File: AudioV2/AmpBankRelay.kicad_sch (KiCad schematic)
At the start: 20 parts, among them K301 AZ850P2-5, K302 AZ850P2-5, K303 AZ850P2-5, K304 AZ850P2-5, U321 TBD62083APG

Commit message: AudioV2: AmpBankSwitch に MCP/ADDR を寄せ、親の SLOT SEL を外す
娘で SEL を出し、縦積み向け ADDR ジャンパと PCB デジタル島・AMP_SEL 取り回しを進める。

Co-authored-by: Cursor <cursoragent@cursor.com>
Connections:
- net CH1_RST: now also U_IO302.27 (GPA6); no longer U_IO302.1 (GPB0)
- net CH1_SET: now also U_IO302.28 (GPA7); no longer U_IO302.21 (GPA0)
- net CH2_RST: now also U_IO302.25 (GPA4); no longer U_IO302.2 (GPB1)
- net CH2_SET: now also U_IO302.26 (GPA5); no longer U_IO302.22 (GPA1)
- net CH3_RST: now also U_IO302.23 (GPA2); no longer U_IO302.3 (GPB2)
- net CH3_SET: now also U_IO302.24 (GPA3); no longer U_IO302.23 (GPA2)
- net CH4_RST: now also U_IO302.21 (GPA0); no longer U_IO302.4 (GPB3)
- net CH4_SET: now also U_IO302.22 (GPA1); no longer U_IO302.24 (GPA3)

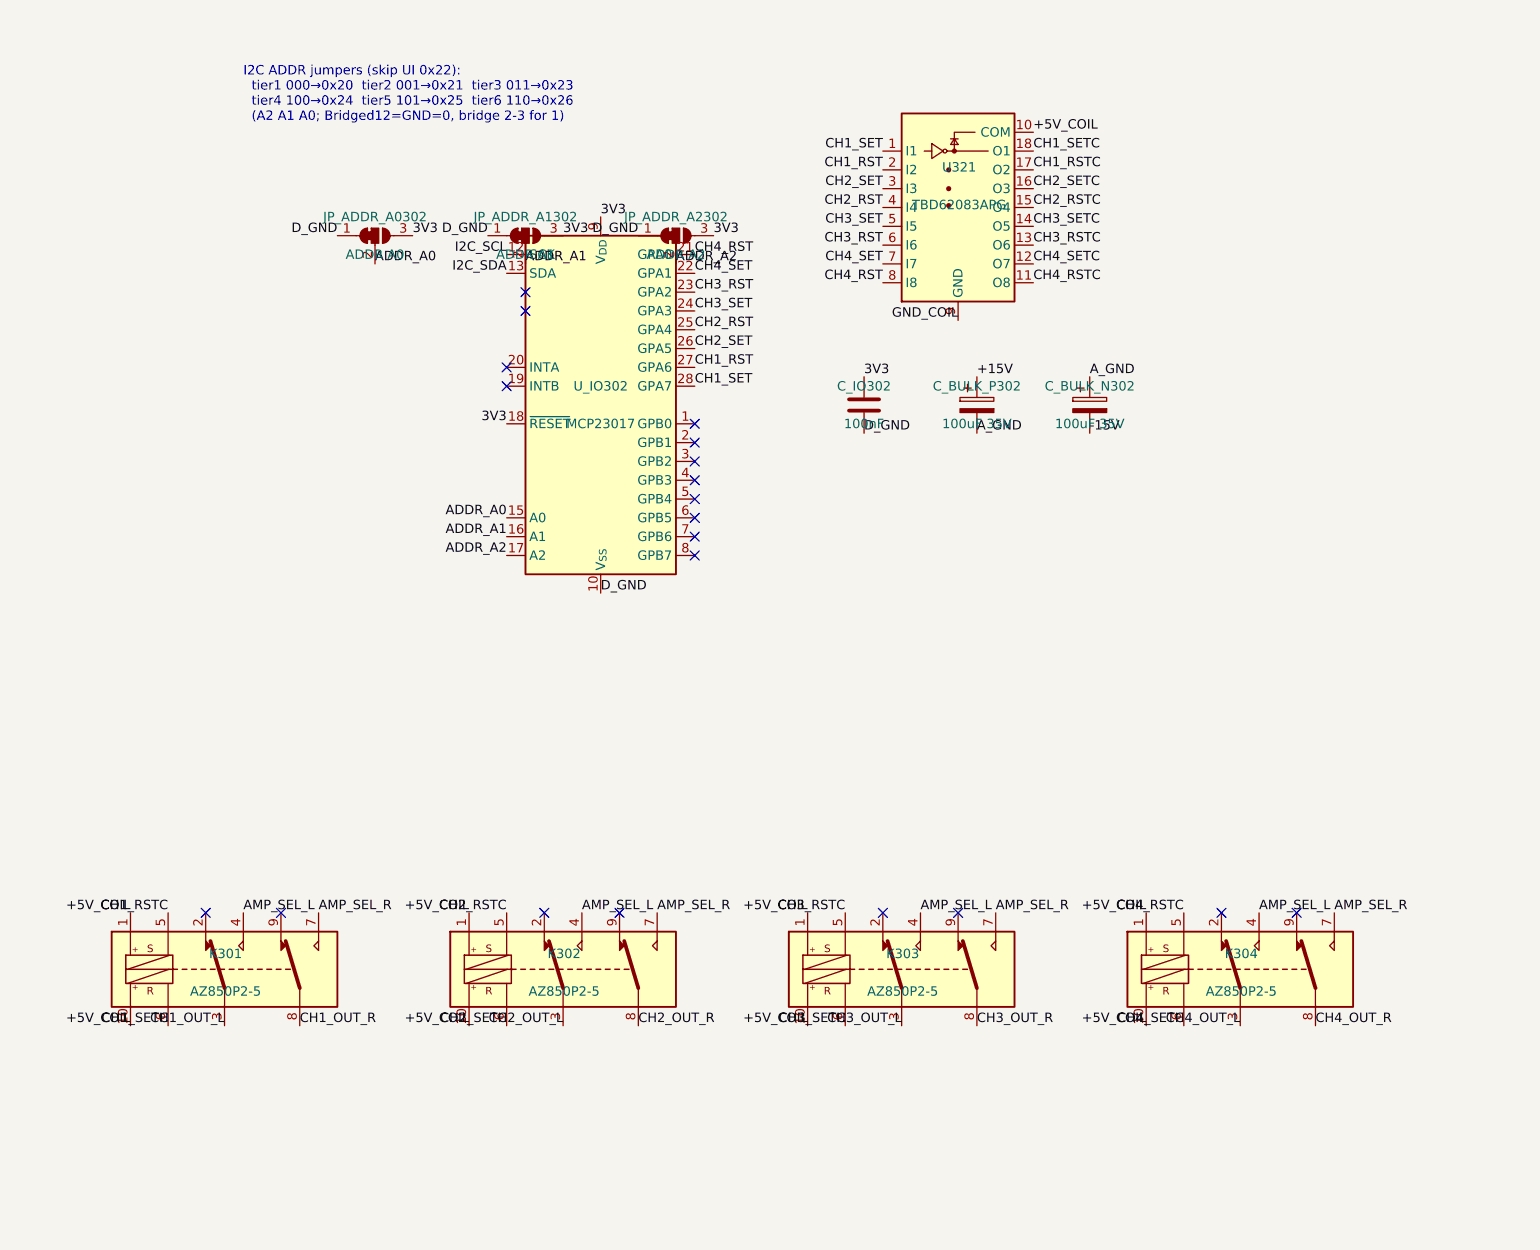
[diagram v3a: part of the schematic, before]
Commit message: AudioV2: AmpBankRelay の配置・配線と回路図更新を保存
CH を横並び＋K 南向きに整え、局所配線まで閉じた。外形拡幅と
回路図側のラベル／接続の直しも同梱する。

Co-authored-by: Cursor <cursoragent@cursor.com>
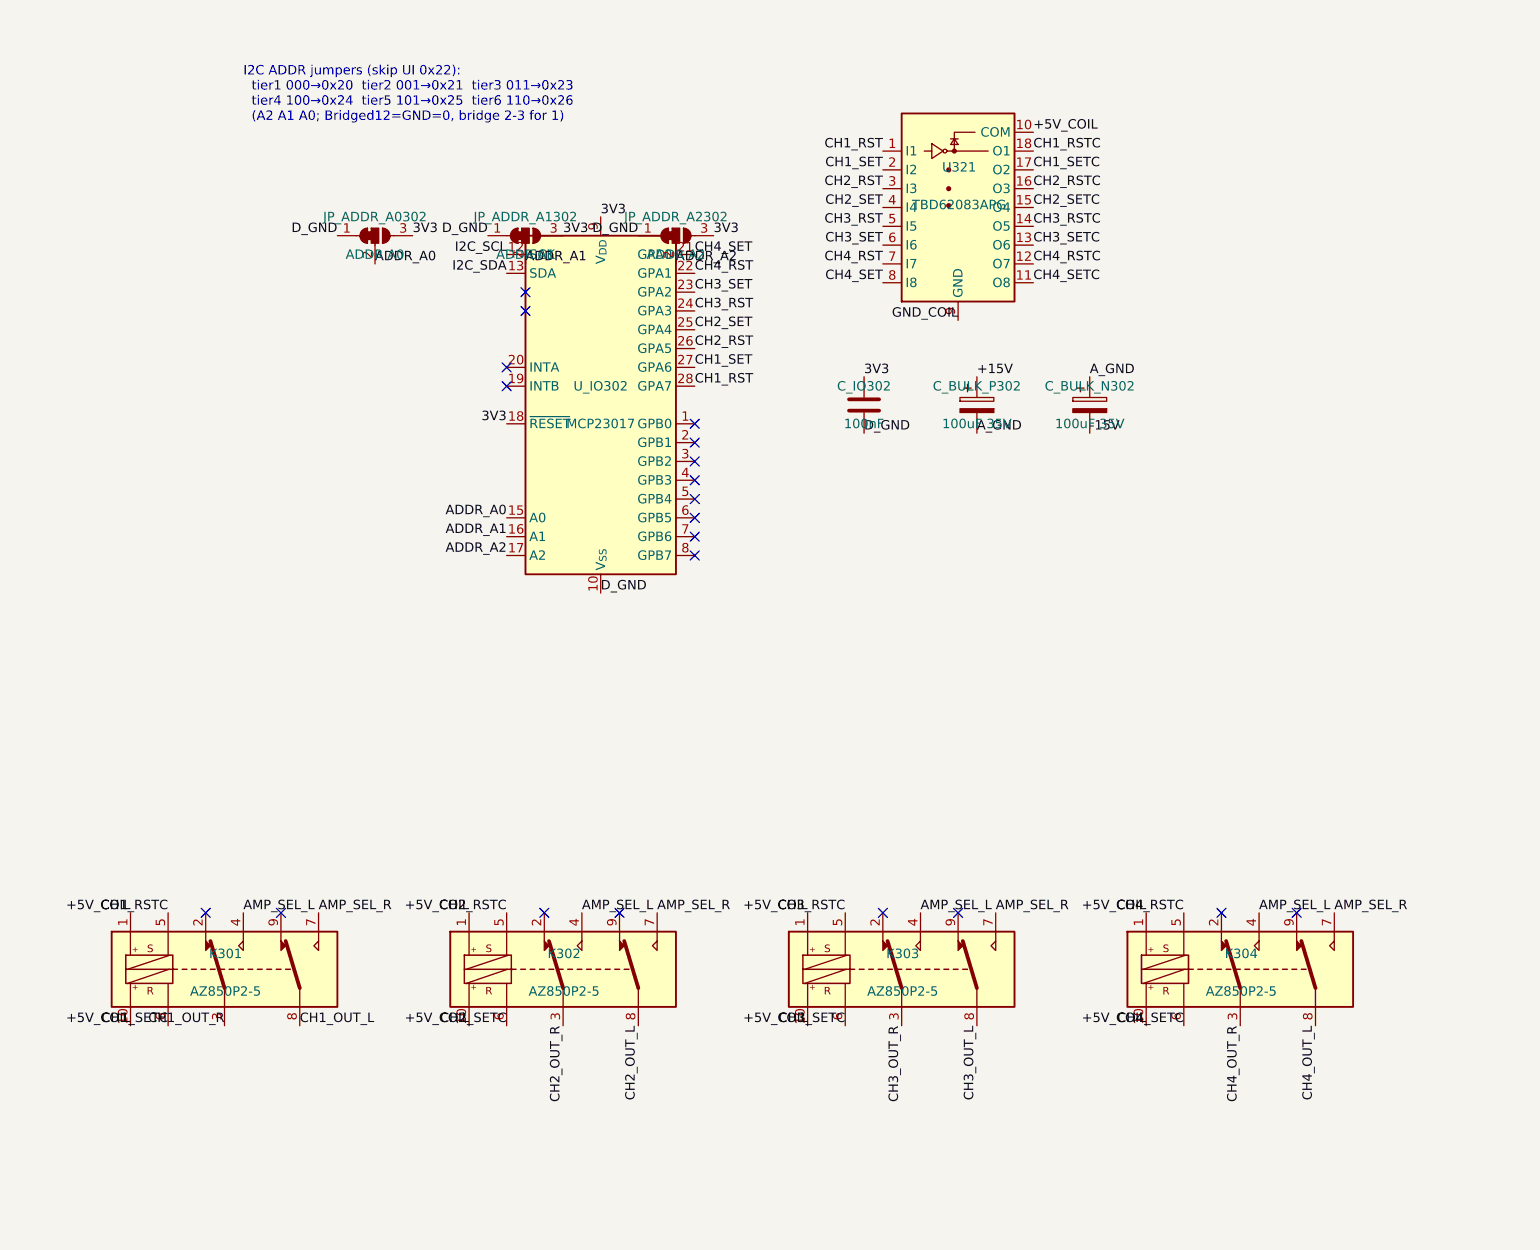
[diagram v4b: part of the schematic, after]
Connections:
- net CH1_OUT_L: now also K301.8; no longer K301.3
- net CH1_OUT_R: now also K301.3; no longer K301.8
- net CH1_RST: now also U321.1 (I1), U_IO302.28 (GPA7); no longer U321.2 (I2), U_IO302.27 (GPA6)
- net CH1_RSTC: now also U321.18 (O1); no longer U321.17 (O2)
- net CH1_SET: now also U321.2 (I2), U_IO302.27 (GPA6); no longer U321.1 (I1), U_IO302.28 (GPA7)
- net CH1_SETC: now also U321.17 (O2); no longer U321.18 (O1)
- net CH2_OUT_L: now also K302.8; no longer K302.3
- net CH2_OUT_R: now also K302.3; no longer K302.8
- net CH2_RST: now also U321.3 (I3), U_IO302.26 (GPA5); no longer U321.4 (I4), U_IO302.25 (GPA4)
- net CH2_RSTC: now also U321.16 (O3); no longer U321.15 (O4)
- net CH2_SET: now also U321.4 (I4), U_IO302.25 (GPA4); no longer U321.3 (I3), U_IO302.26 (GPA5)
- net CH2_SETC: now also U321.15 (O4); no longer U321.16 (O3)
- net CH3_OUT_L: now also K303.8; no longer K303.3
- net CH3_OUT_R: now also K303.3; no longer K303.8
- net CH3_RST: now also U321.5 (I5), U_IO302.24 (GPA3); no longer U321.6 (I6), U_IO302.23 (GPA2)
- net CH3_RSTC: now also U321.14 (O5); no longer U321.13 (O6)
- net CH3_SET: now also U321.6 (I6), U_IO302.23 (GPA2); no longer U321.5 (I5), U_IO302.24 (GPA3)
- net CH3_SETC: now also U321.13 (O6); no longer U321.14 (O5)
- net CH4_OUT_L: now also K304.8; no longer K304.3
- net CH4_OUT_R: now also K304.3; no longer K304.8
- net CH4_RST: now also U321.7 (I7), U_IO302.22 (GPA1); no longer U321.8 (I8), U_IO302.21 (GPA0)
- net CH4_RSTC: now also U321.12 (O7); no longer U321.11 (O8)
- net CH4_SET: now also U321.8 (I8), U_IO302.21 (GPA0); no longer U321.7 (I7), U_IO302.22 (GPA1)
- net CH4_SETC: now also U321.11 (O8); no longer U321.12 (O7)
